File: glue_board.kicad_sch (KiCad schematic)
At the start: 39 parts, among them CN1 CH3, CN11 CH4, CN13 CH3, CN15 CH1, CN2 CH3, CN3 CH3, CN4 CH3, CN8 CH4, J1 H3, J10 H2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

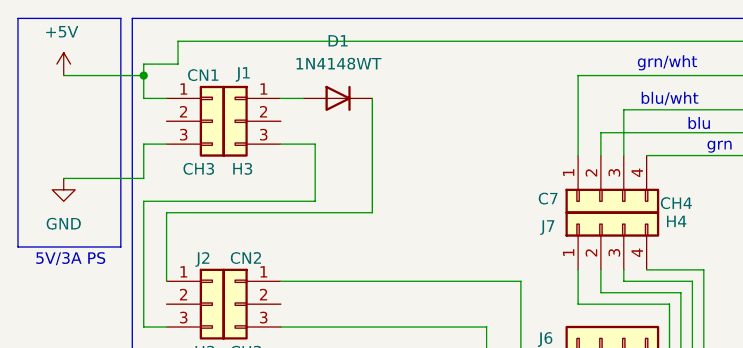
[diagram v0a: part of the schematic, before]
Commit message: update to pclient and added device for logging, updated the way BME280 samples and bumped version
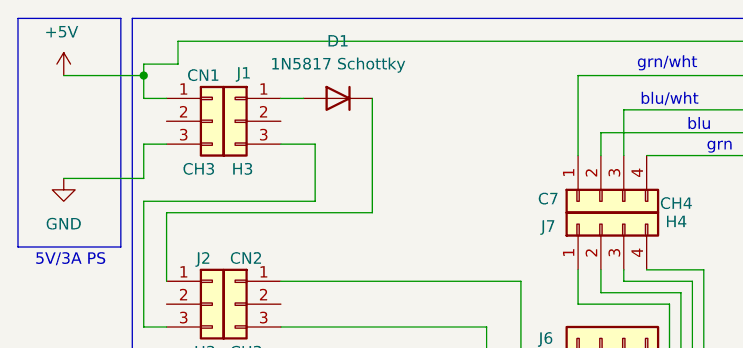
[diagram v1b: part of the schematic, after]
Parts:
- D1: value 1N4148WT -> 1N5817 Schottky
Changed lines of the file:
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@@
 			)
 		)
-		(property "Value" "1N4148WT"
+		(property "Value" "1N5817 Schottky"
 			(at 50.8 17.78 0)
 			(effects
